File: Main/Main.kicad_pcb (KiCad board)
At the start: 4 copper layers, 76.2 x 64.9 mm, 96 parts, among them J1 USB_B_Micro, J2 XT60, J3 Conn_01x03, J4 Conn_01x03, J5 Conn_01x03, J6 Conn_01x03, J7 MSD-4-A, Q2 Si2301CDS, SW1 SW_Push, SW2 SW_Push, U1 RP2350A-QFN60, U10 LM75B, U11 MCS1802GS-50-Z, U12 MCS1802GS-50-Z, U13 MCS1802GS-50-Z, U15 AP62150WU, U2 W25Q128JVS, U3 AMS1117-3.3, U4 MMC5983MA, U5 ICM-42688-P, U6 INA226, U7 KX134-1211, U8 MS5611-01BA, U9 MCS1802GS-50-Z, Y1 ABM8-272-T3

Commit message: more layout updates and small fixes
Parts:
- D1: value LED -> RED_LED
- D2: value LED -> BLUE_LED
- D3: value LED -> GREEN_LED
- moved C26 108.7 mm to (125.5, 110.0), turned to -90 degrees
- moved C25 106.4 mm to (121.5, 110.5), turned to -90 degrees
- moved C22 106.2 mm to (123.0, 103.0), turned to 180 degrees
- moved C23 103.3 mm to (123.0, 97.0), turned to 180 degrees
- moved R5 97.8 mm to (107.0, 125.0)
- moved C27 95.4 mm to (112.4, 108.1), turned to -90 degrees
- moved C37 95.1 mm to (106.5, 118.0)
- moved C19 92.2 mm to (103.2, 118.0), turned to -90 degrees
- moved C30 91.4 mm to (115.8, 97.8), turned to 180 degrees
- moved C38 90.8 mm to (104.2, 118.0), turned to -90 degrees
- moved R16 90.3 mm to (104.5, 120.8), turned to 90 degrees
- moved C29 90.2 mm to (113.8, 97.8)
- moved R9 89.9 mm to (105.5, 120.8), turned to -90 degrees
- moved R4 89.7 mm to (93.0, 125.0)
- moved C11 89.6 mm to (101.8, 105.6), turned to -45 degrees
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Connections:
- C29 pad 2: Net-(C29-Pad2) -> GND
- C30 pad 2: Net-(C29-Pad2) -> GND
- J2 pad 2: VIN -> Net-(J2-Pin_2)
- R13 pad 1: GND -> VIN
- R13 pad 2: VSS -> Net-(J2-Pin_2)
- U6 pad 10: VSS -> Net-(J2-Pin_2)
- U6 pad 8: GND -> Net-(J2-Pin_2)
- U6 pad 9: GND -> VIN
- U7 pad 1: ACCEL_SDO/ADDR -> SPI_SD0
- U7 pad 2: ACCEL_SDI/SDA -> SPI_SDI
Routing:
- net +3.3V: track 12.1 -> 27.1 mm, vias 0 -> 1
- net GND: track 0.18 -> 14.0 mm, vias 2 -> 4
- net Net-(U1-XIN): track 0.00 -> 10.3 mm
- net Net-(J2-Pin_2): track 0.00 -> 5.61 mm
- net Net-(C17-Pad2): track 0.00 -> 4.96 mm
- net Net-(J7-DAT2): track 0.00 -> 3.89 mm, vias 0 -> 1
- net VIN: track 0.00 -> 3.44 mm
- net SPI_SCLK2: track 0.00 -> 2.99 mm, vias 0 -> 1
- net SPI_SDI2: track 0.00 -> 2.95 mm, vias 0 -> 1
- net SPI_SDO2: track 0.00 -> 2.78 mm, vias 0 -> 1
- net SD_CD: track 0.00 -> 2.74 mm, vias 0 -> 1
- net Net-(J7-DAT1): track 0.00 -> 2.74 mm, vias 0 -> 1
- net Net-(U1-XOUT): track 0.00 -> 1.93 mm
- net SD_ChipSelect: track 0.00 -> 1.79 mm
- net Net-(D3-A): track 0.00 -> 1.55 mm
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- added copper zone on In1.Cu, net GND
- added copper zone on F.Cu, net Net-(J2-Pin_2)

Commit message: more layout updates
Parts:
- moved R7 54.8 mm to (97.1, 93.4), turned to -45 degrees
- moved R8 53.7 mm to (96.4, 94.1), turned to -45 degrees
- moved C22 36.3 mm to (159.2, 100.0)
- moved C23 36.3 mm to (159.2, 94.0)
- moved C25 36.3 mm to (157.7, 107.5)
- moved C26 36.3 mm to (161.7, 107.0)
- moved C27 36.3 mm to (148.6, 105.1)
- moved C29 36.3 mm to (149.9, 94.8)
- moved U4 36.3 mm to (159.2, 97.0)
- moved U5 36.3 mm to (151.2, 97.0)
- moved U7 36.3 mm to (159.7, 106.8)
- moved U8 36.3 mm to (151.2, 106.4)
- moved C30 36.3 mm to (151.9, 94.8)
- moved C31 33.9 mm to (120.0, 84.8), turned to 90 degrees
- moved C34 25.1 mm to (106.5, 85.0), turned to 90 degrees
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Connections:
- U1 pad 32: unconnected-(U1-GPIO20-Pad32) -> SDA
- U1 pad 33: unconnected-(U1-GPIO21-Pad33) -> SCL
- U1 pad 40: unconnected-(U1-GPIO26_ADC0-Pad40) -> Vout1
- U1 pad 41: unconnected-(U1-GPIO27_ADC1-Pad41) -> Vout2
- U1 pad 42: unconnected-(U1-GPIO28_ADC2-Pad42) -> Vout4
- U1 pad 43: unconnected-(U1-GPIO29_ADC3-Pad43) -> Vout3
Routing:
- net GND: track 14.0 -> 82.8 mm, vias 4 -> 39
- net +3.3V: track 27.1 -> 77.0 mm, vias 1 -> 10
- net Vout1: track 0.00 -> 34.6 mm
- net Net-(U1-RUN): track 0.00 -> 31.0 mm, vias 0 -> 2
- net Vout2: track 0.00 -> 22.1 mm
- net /QSPI_SS: track 7.25 -> 27.3 mm
- net Vout3: track 0.00 -> 19.5 mm
- net Vout4: track 0.00 -> 17.5 mm
- net /USB_D+: track 12.3 -> 27.0 mm
- net /USB_D-: track 12.9 -> 27.6 mm
- net SDA: track 0.00 -> 5.92 mm, vias 0 -> 3
- net SCL: track 0.00 -> 5.70 mm, vias 0 -> 3
- net +1V1: track 4.52 -> 9.46 mm
- net VBUS: track 21.6 -> 16.7 mm, vias 0 -> 9
- net Net-(U1-VREG_LX): track 0.00 -> 4.05 mm
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- added copper zone on In2.Cu, net +3.3V
- added copper zone on F.Cu, net GND
- added copper zone on F.Cu, net VBUS
- added copper zone on In2.Cu, net VBUS
- added copper zone on F.Cu, net VIN
- added copper zone on In2.Cu, net VIN
- added copper zone on F.Cu, net current -4
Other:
- board text added: "SIG, GND, PWR, SIG Stackup"

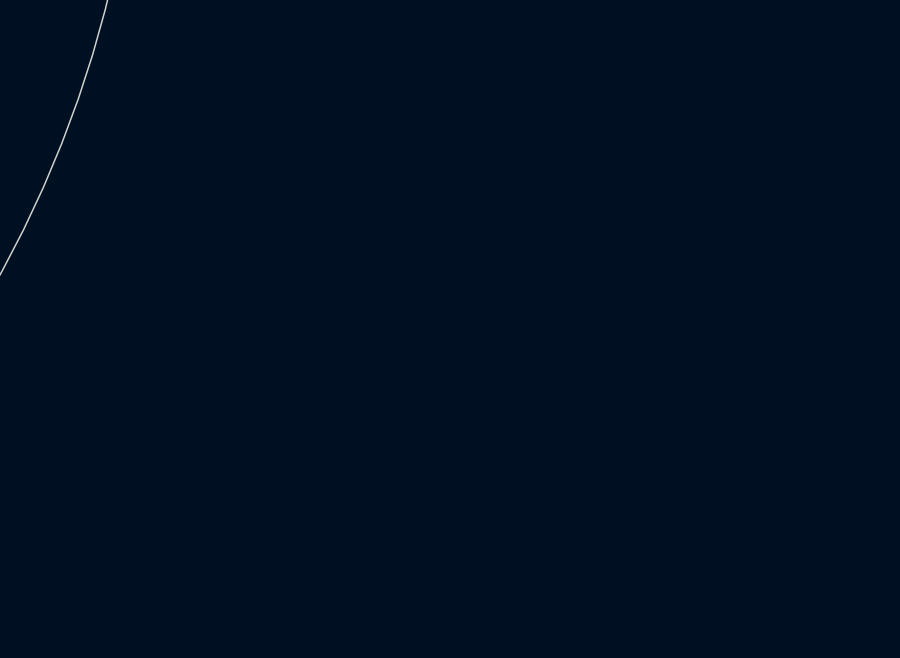
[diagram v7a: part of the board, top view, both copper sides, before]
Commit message: updated layout
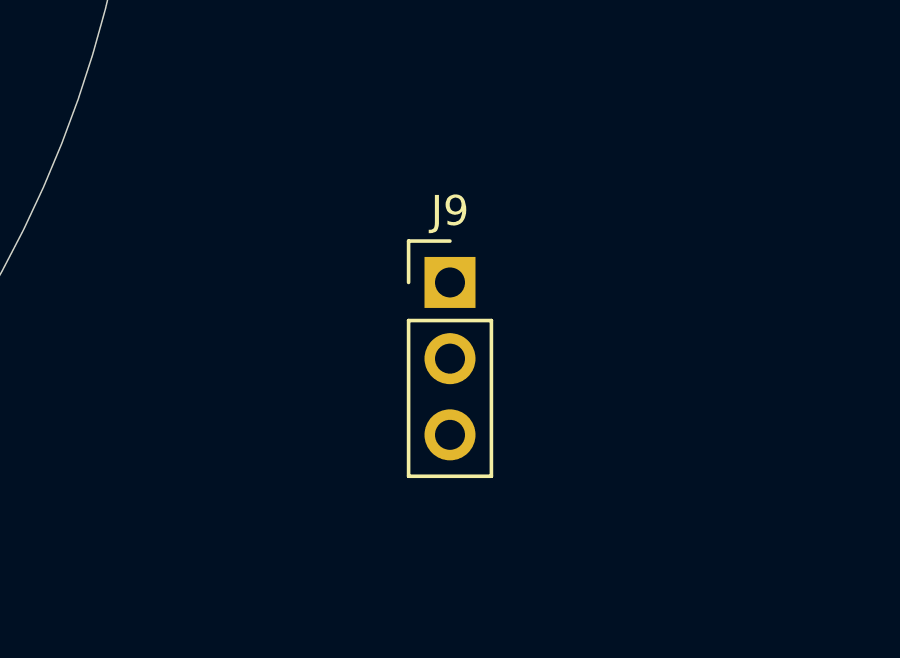
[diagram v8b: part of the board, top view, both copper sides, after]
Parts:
- added J9: Conn_01x03, Connector_PinHeader_2.54mm:PinHeader_1x03_P2.54mm_Vertical, F.Cu at (148.3, 118.5)
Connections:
- U1 pad 24: unconnected-(U1-SWCLK-Pad24) -> Net-(J9-Pin_3)
- U1 pad 25: unconnected-(U1-SWDIO-Pad25) -> Net-(J9-Pin_2)
